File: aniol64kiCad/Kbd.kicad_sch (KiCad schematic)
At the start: 24 parts, among them J5 Buzzer, U2 74LS14, U4 74LS32, U5 74LS08

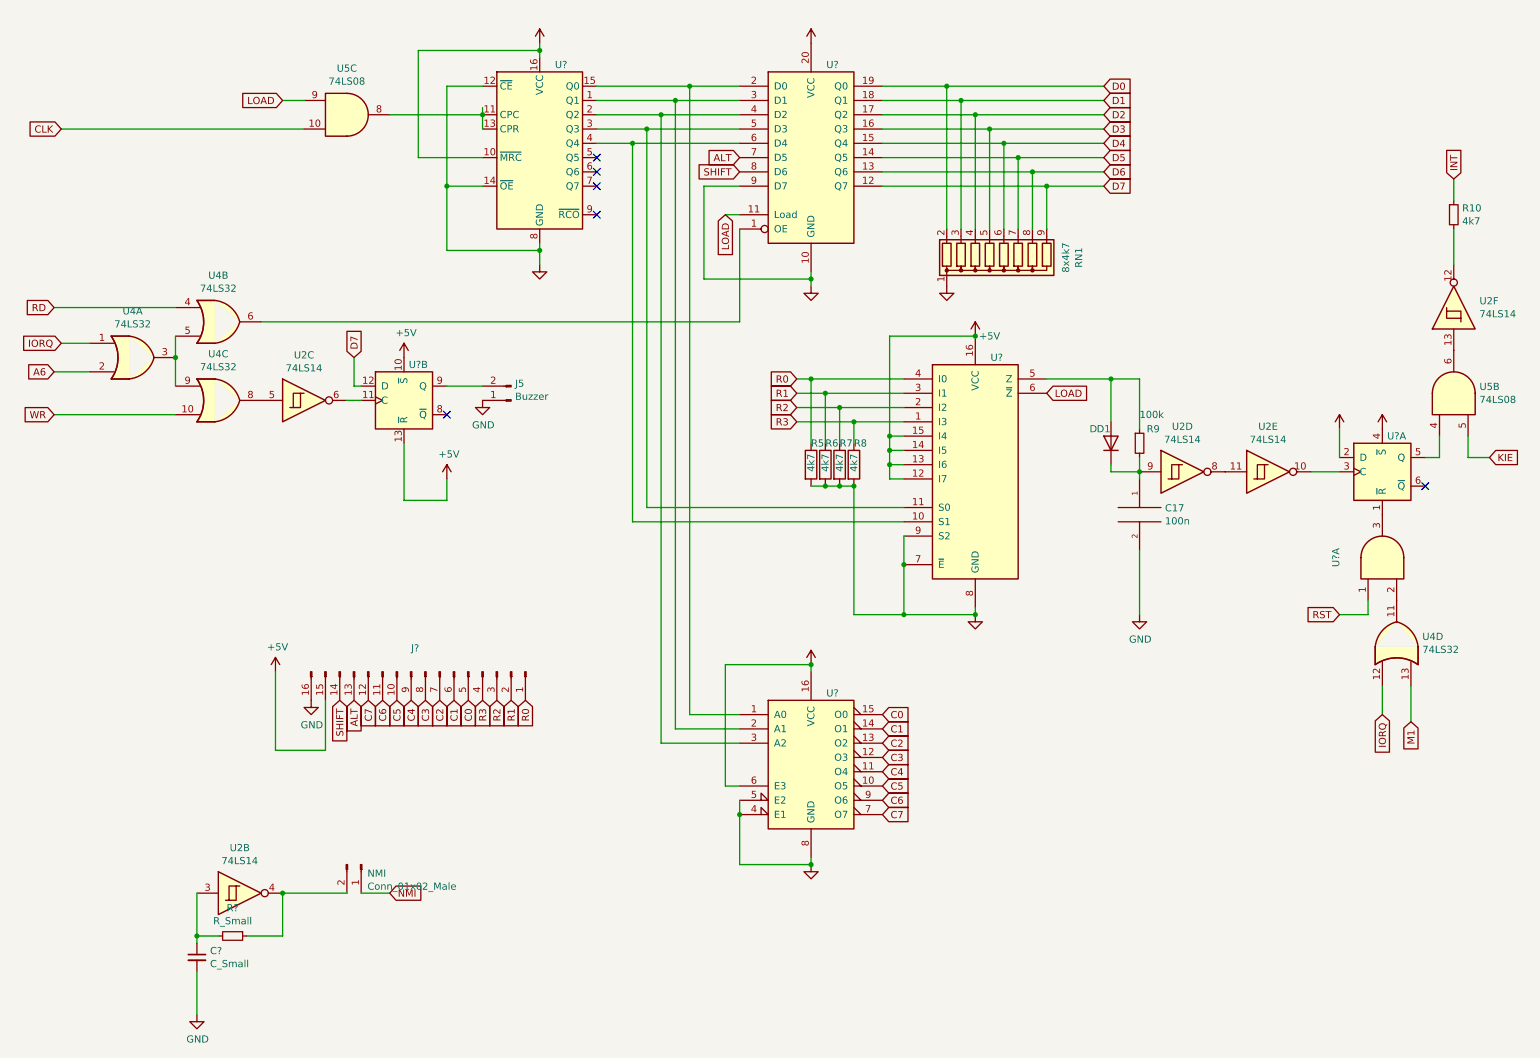
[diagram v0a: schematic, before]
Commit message: added scrolling in edit
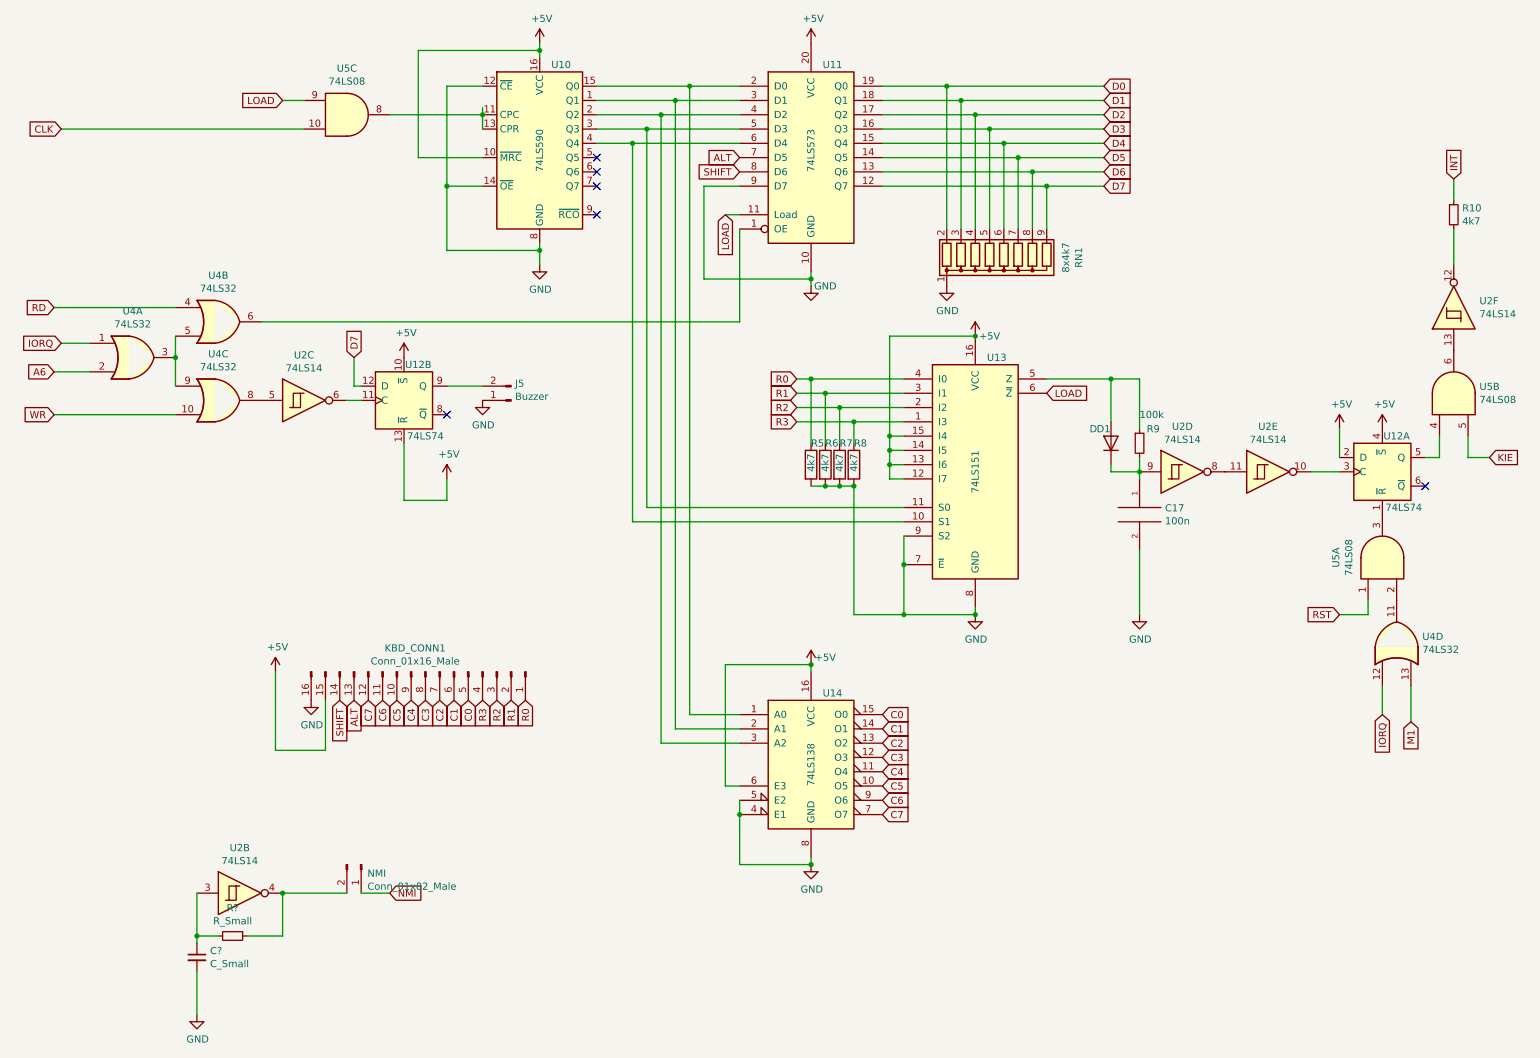
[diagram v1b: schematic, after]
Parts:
- KBD_CONN1: renamed from J?; value (none) -> Conn_01x16_Male; footprint (none) -> Connector_PinHeader_2.54mm:PinHeader_1x16_P2.54mm_Vertical
- U10: renamed from U?; value (none) -> 74LS590; footprint (none) -> Package_DIP:DIP-16_W7.62mm_Socket
- U11: renamed from U?; value (none) -> 74LS573; footprint (none) -> Package_DIP:DIP-20_W7.62mm_Socket
- U12: renamed from U?; value (none) -> 74LS74; footprint (none) -> Package_DIP:DIP-14_W7.62mm_Socket
- U13: renamed from U?; value (none) -> 74LS151; footprint (none) -> Package_DIP:DIP-16_W7.62mm_Socket
- U14: renamed from U?; value (none) -> 74LS138; footprint (none) -> Package_DIP:DIP-16_W7.62mm_Socket
- U5: renamed from U?; value (none) -> 74LS08; footprint (none) -> Package_DIP:DIP-14_W7.62mm_Socket
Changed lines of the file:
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@@
   (symbol (lib_id "Connector:Conn_01x16_Male") (at 87.63 130.81 270) (unit 1)
     (in_bom yes) (on_board yes)
-    (property "Reference" "J?" (id 0) (at 85.8012 126.619 90))
-    (property "Value" "" (id 1) (at 85.8012 128.9304 90))
-    (property "Footprint" "" (id 2) (at 87.63 130.81 0)
+    (property "Reference" "KBD_CONN1" (id 0) (at 85.8012 126.619 90))
+    (property "Value" "Conn_01x16_Male" (id 1) (at 85.8012 128.9304 90))
+    (property "Footprint" "Connector_PinHeader_2.54mm:PinHeader_1x16_P2.54mm_Vertical" (id 2) (at 87.63 130.81 0)
       (effects (font (size 1.27 1.27)) hide)
     )
@@
   (symbol (lib_id "power:+5V") (at 156.21 129.54 0) (unit 1)
     (in_bom yes) (on_board yes)
-    (property "Reference" "#PWR?" (id 0) (at 156.21 133.35 0)
-      (effects (font (size 1.27 1.27)) hide)
-    )
-    (property "Value" "" (id 1) (at 158.75 128.27 0))
+    (property "Reference" "#PWR029" (id 0) (at 156.21 133.35 0)
+      (effects (font (size 1.27 1.27)) hide)
+    )
+    (property "Value" "+5V" (id 1) (at 158.75 128.27 0))
     (property "Footprint" "" (id 2) (at 156.21 129.54 0)
       (effects (font (size 1.27 1.27)) hide)
@@
   (symbol (lib_id "power:GND") (at 156.21 165.1 0) (unit 1)
     (in_bom yes) (on_board yes)
-    (property "Reference" "#PWR?" (id 0) (at 156.21 171.45 0)
-      (effects (font (size 1.27 1.27)) hide)
-    )
-    (property "Value" "" (id 1) (at 156.337 169.4942 0))
+    (property "Reference" "#PWR030" (id 0) (at 156.21 171.45 0)
+      (effects (font (size 1.27 1.27)) hide)
+    )
+    (property "Value" "GND" (id 1) (at 156.337 169.4942 0))
     (property "Footprint" "" (id 2) (at 156.21 165.1 0)
       (effects (font (size 1.27 1.27)) hide)
@@
   (symbol (lib_id "power:GND") (at 185.42 120.65 0) (unit 1)
     (in_bom yes) (on_board yes)
-    (property "Reference" "#PWR?" (id 0) (at 185.42 127 0)
-      (effects (font (size 1.27 1.27)) hide)
-    )
-    (property "Value" "" (id 1) (at 185.547 125.0442 0))
+    (property "Reference" "#PWR032" (id 0) (at 185.42 127 0)
+      (effects (font (size 1.27 1.27)) hide)
+    )
+    (property "Value" "GND" (id 1) (at 185.547 125.0442 0))
     (property "Footprint" "" (id 2) (at 185.42 120.65 0)
       (effects (font (size 1.27 1.27)) hide)
@@
   (symbol (lib_id "74xx:74LS138") (at 156.21 146.05 0) (unit 1)
     (in_bom yes) (on_board yes)
-    (property "Reference" "U?" (id 0) (at 160.02 134.62 0))
-    (property "Value" "" (id 1) (at 156.21 147.32 90))
-    (property "Footprint" "" (id 2) (at 156.21 146.05 0)
+    (property "Reference" "U14" (id 0) (at 160.02 134.62 0))
+    (property "Value" "74LS138" (id 1) (at 156.21 147.32 90))
+    (property "Footprint" "Package_DIP:DIP-16_W7.62mm_Socket" (id 2) (at 156.21 146.05 0)
       (effects (font (size 1.27 1.27)) hide)
     )
@@
   (symbol (lib_id "74xx:74LS151") (at 185.42 93.98 0) (unit 1)
     (in_bom yes) (on_board yes)
-    (property "Reference" "U?" (id 0) (at 189.23 74.93 0))
-    (property "Value" "" (id 1) (at 185.42 95.25 90))
-    (property "Footprint" "" (id 2) (at 185.42 93.98 0)
+    (property "Reference" "U13" (id 0) (at 189.23 74.93 0))
+    (property "Value" "74LS151" (id 1) (at 185.42 95.25 90))
+    (property "Footprint" "Package_DIP:DIP-16_W7.62mm_Socket" (id 2) (at 185.42 93.98 0)
       (effects (font (size 1.27 1.27)) hide)
     )
@@
   (symbol (lib_id "power:GND") (at 107.95 58.42 0) (unit 1)
     (in_bom yes) (on_board yes)
-    (property "Reference" "#PWR?" (id 0) (at 107.95 64.77 0)
-      (effects (font (size 1.27 1.27)) hide)
-    )
-    (property "Value" "" (id 1) (at 108.077 62.8142 0))
+    (property "Reference" "#PWR026" (id 0) (at 107.95 64.77 0)
+      (effects (font (size 1.27 1.27)) hide)
+    )
+    (property "Value" "GND" (id 1) (at 108.077 62.8142 0))
     (property "Footprint" "" (id 2) (at 107.95 58.42 0)
       (effects (font (size 1.27 1.27)) hide)
@@
   (symbol (lib_id "power:+5V") (at 107.95 19.05 0) (unit 1)
     (in_bom yes) (on_board yes)
-    (property "Reference" "#PWR?" (id 0) (at 107.95 22.86 0)
-      (effects (font (size 1.27 1.27)) hide)
-    )
-    (property "Value" "" (id 1) (at 108.331 14.6558 0))
+    (property "Reference" "#PWR025" (id 0) (at 107.95 22.86 0)
+      (effects (font (size 1.27 1.27)) hide)
+    )
+    (property "Value" "+5V" (id 1) (at 108.331 14.6558 0))
     (property "Footprint" "" (id 2) (at 107.95 19.05 0)
       (effects (font (size 1.27 1.27)) hide)
@@
   (symbol (lib_id "74xx:74LS590") (at 107.95 39.37 0) (unit 1)
     (in_bom yes) (on_board yes)
-    (property "Reference" "U?" (id 0) (at 111.76 22.86 0))
-    (property "Value" "" (id 1) (at 107.95 38.1 90))
-    (property "Footprint" "" (id 2) (at 107.95 38.1 0)
+    (property "Reference" "U10" (id 0) (at 111.76 22.86 0))
+    (property "Value" "74LS590" (id 1) (at 107.95 38.1 90))
+    (property "Footprint" "Package_DIP:DIP-16_W7.62mm_Socket" (id 2) (at 107.95 38.1 0)
       (effects (font (size 1.27 1.27)) hide)
     )
@@
   (symbol (lib_id "power:GND") (at 156.21 62.23 0) (unit 1)
     (in_bom yes) (on_board yes)
-    (property "Reference" "#PWR?" (id 0) (at 156.21 68.58 0)
-      (effects (font (size 1.27 1.27)) hide)
-    )
-    (property "Value" "" (id 1) (at 158.75 62.23 0))
+    (property "Reference" "#PWR028" (id 0) (at 156.21 68.58 0)
+      (effects (font (size 1.27 1.27)) hide)
+    )
+    (property "Value" "GND" (id 1) (at 158.75 62.23 0))
     (property "Footprint" "" (id 2) (at 156.21 62.23 0)
       (effects (font (size 1.27 1.27)) hide)
@@
   (symbol (lib_id "power:+5V") (at 156.21 19.05 0) (unit 1)
     (in_bom yes) (on_board yes)
-    (property "Reference" "#PWR?" (id 0) (at 156.21 22.86 0)
-      (effects (font (size 1.27 1.27)) hide)
-    )
-    (property "Value" "" (id 1) (at 156.591 14.6558 0))
+    (property "Reference" "#PWR027" (id 0) (at 156.21 22.86 0)
+      (effects (font (size 1.27 1.27)) hide)
+    )
+    (property "Value" "+5V" (id 1) (at 156.591 14.6558 0))
     (property "Footprint" "" (id 2) (at 156.21 19.05 0)
       (effects (font (size 1.27 1.27)) hide)
@@
   (symbol (lib_id "74xx:74LS573") (at 156.21 39.37 0) (unit 1)
     (in_bom yes) (on_board yes)
-    (property "Reference" "U?" (id 0) (at 160.02 22.86 0))
-    (property "Value" "" (id 1) (at 156.21 38.1 90))
-    (property "Footprint" "" (id 2) (at 156.21 39.37 0)
+    (property "Reference" "U11" (id 0) (at 160.02 22.86 0))
+    (property "Value" "74LS573" (id 1) (at 156.21 38.1 90))
+    (property "Footprint" "Package_DIP:DIP-20_W7.62mm_Socket" (id 2) (at 156.21 39.37 0)
       (effects (font (size 1.27 1.27)) hide)
     )
@@
   (symbol (lib_id "74xx:74LS74") (at 257.81 95.25 0) (unit 1)
     (in_bom yes) (on_board yes)
-    (property "Reference" "U?" (id 0) (at 260.35 88.9 0))
-    (property "Value" "" (id 1) (at 261.62 101.6 0))
-    (property "Footprint" "" (id 2) (at 257.81 95.25 0)
+    (property "Reference" "U12" (id 0) (at 260.35 88.9 0))
+    (property "Value" "74LS74" (id 1) (at 261.62 101.6 0))
+    (property "Footprint" "Package_DIP:DIP-14_W7.62mm_Socket" (id 2) (at 257.81 95.25 0)
       (effects (font (size 1.27 1.27)) hide)
     )
@@
   (symbol (lib_id "74xx:74LS08") (at 257.81 110.49 90) (unit 1)
     (in_bom yes) (on_board yes)
-    (property "Reference" "U?" (id 0) (at 249.555 110.49 0))
-    (property "Value" "" (id 1) (at 251.8664 110.49 0))
-    (property "Footprint" "" (id 2) (at 257.81 110.49 0)
+    (property "Reference" "U5" (id 0) (at 249.555 110.49 0))
+    (property "Value" "74LS08" (id 1) (at 251.8664 110.49 0))
+    (property "Footprint" "Package_DIP:DIP-14_W7.62mm_Socket" (id 2) (at 257.81 110.49 0)
       (effects (font (size 1.27 1.27)) hide)
     )
@@
   (symbol (lib_id "power:+5V") (at 257.81 87.63 0) (unit 1)
     (in_bom yes) (on_board yes)
-    (property "Reference" "#PWR?" (id 0) (at 257.81 91.44 0)
-      (effects (font (size 1.27 1.27)) hide)
-    )
-    (property "Value" "" (id 1) (at 258.191 83.2358 0))
+    (property "Reference" "#PWR036" (id 0) (at 257.81 91.44 0)
+      (effects (font (size 1.27 1.27)) hide)
+    )
+    (property "Value" "+5V" (id 1) (at 258.191 83.2358 0))
     (property "Footprint" "" (id 2) (at 257.81 87.63 0)
       (effects (font (size 1.27 1.27)) hide)
@@
   (symbol (lib_id "power:+5V") (at 250.19 87.63 0) (unit 1)
     (in_bom yes) (on_board yes)
-    (property "Reference" "#PWR?" (id 0) (at 250.19 91.44 0)
-      (effects (font (size 1.27 1.27)) hide)
-    )
-    (property "Value" "" (id 1) (at 250.571 83.2358 0))
+    (property "Reference" "#PWR035" (id 0) (at 250.19 91.44 0)
+      (effects (font (size 1.27 1.27)) hide)
+    )
+    (property "Value" "+5V" (id 1) (at 250.571 83.2358 0))
     (property "Footprint" "" (id 2) (at 250.19 87.63 0)
       (effects (font (size 1.27 1.27)) hide)
@@
   (symbol (lib_id "74xx:74LS74") (at 83.82 82.55 0) (unit 2)
     (in_bom yes) (on_board yes)
-    (property "Reference" "U?" (id 0) (at 86.36 76.2 0))
-    (property "Value" "" (id 1) (at 87.63 88.9 0))
-    (property "Footprint" "" (id 2) (at 83.82 82.55 0)
+    (property "Reference" "U12" (id 0) (at 86.36 76.2 0))
+    (property "Value" "74LS74" (id 1) (at 87.63 88.9 0))
+    (property "Footprint" "Package_DIP:DIP-14_W7.62mm_Socket" (id 2) (at 83.82 82.55 0)
       (effects (font (size 1.27 1.27)) hide)
     )
@@
   (symbol (lib_id "power:GND") (at 180.34 62.23 0) (unit 1)
     (in_bom yes) (on_board yes)
-    (property "Reference" "#PWR?" (id 0) (at 180.34 68.58 0)
-      (effects (font (size 1.27 1.27)) hide)
-    )
-    (property "Value" "" (id 1) (at 180.467 66.6242 0))
+    (property "Reference" "#PWR033" (id 0) (at 180.34 68.58 0)
+      (effects (font (size 1.27 1.27)) hide)
+    )
+    (property "Value" "GND" (id 1) (at 180.467 66.6242 0))
     (property "Footprint" "" (id 2) (at 180.34 62.23 0)
       (effects (font (size 1.27 1.27)) hide)
